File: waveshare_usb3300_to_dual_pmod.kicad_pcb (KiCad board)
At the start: 2 copper layers, 24.8 x 41.3 mm, 4 parts, among them J1 Conn_01x02_Pin, J2 PMOD, J3 PMOD, J4 Conn_02x10_Top_Bottom

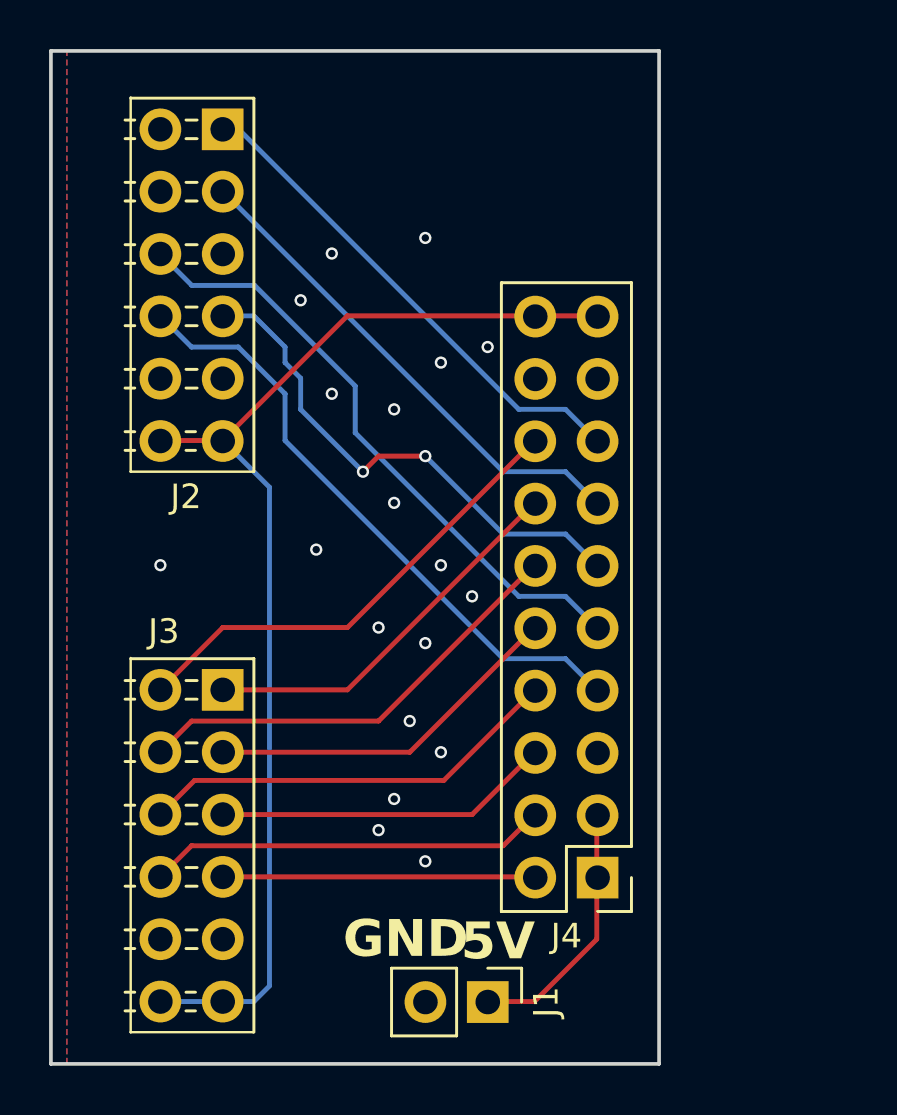
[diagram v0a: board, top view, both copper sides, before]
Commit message: waveshare_usb3300_to_dual_pmod: changed j4 footprint, resize PCB
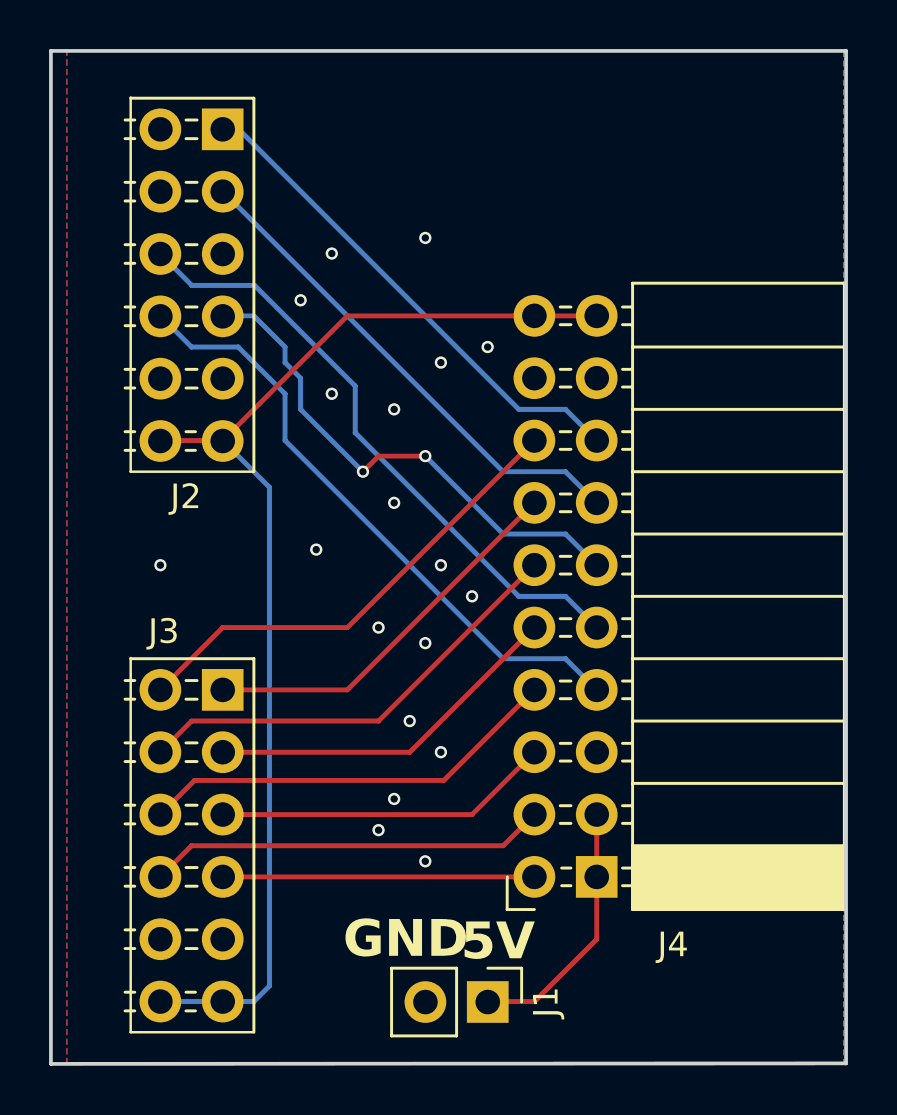
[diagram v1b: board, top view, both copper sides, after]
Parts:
- J4: footprint Connector_PinHeader_2.54mm:PinHeader_2x10_P2.54mm_Vertical -> usb3300_connector:PinSocket_2x10_P2.54mm_Horizontal
- moved J4 2.58 mm to (56.7, 56.7)
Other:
- board size 24.8 x 41.3 mm -> 32.4 x 41.3 mm

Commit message: waveshare_usb3300_to_dual_pmod.kicad_pcb: reworks GND (thanks Goran!)
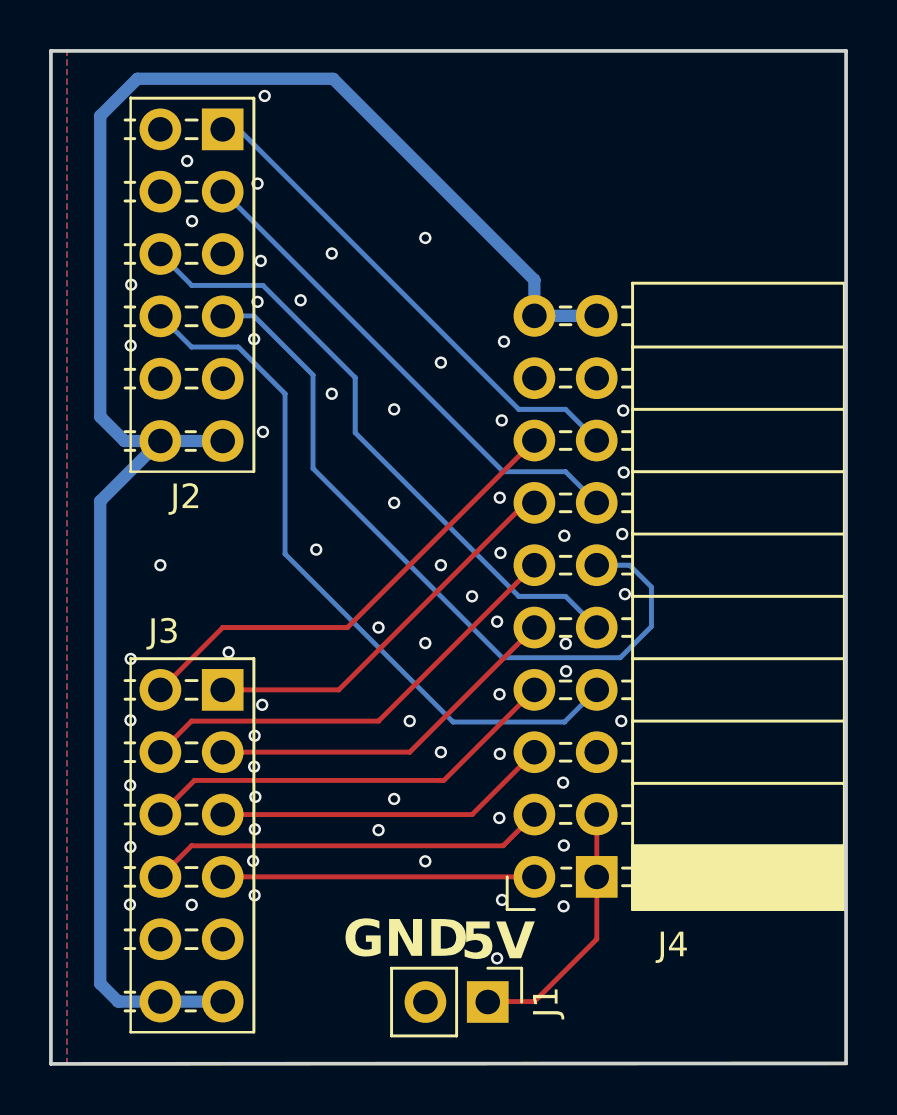
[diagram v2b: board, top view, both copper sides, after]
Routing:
- net +3.3V: track 47.6 -> 71.8 mm
- net DIR: track 21.1 -> 30.2 mm, vias 2 -> 0
- net RESET: track 25.2 -> 29.0 mm
- net GND: vias 19 -> 63

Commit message: waveshare_usb3300_to_dual_pmod.kicad_pcb: updates clock routing (thanks Goran)
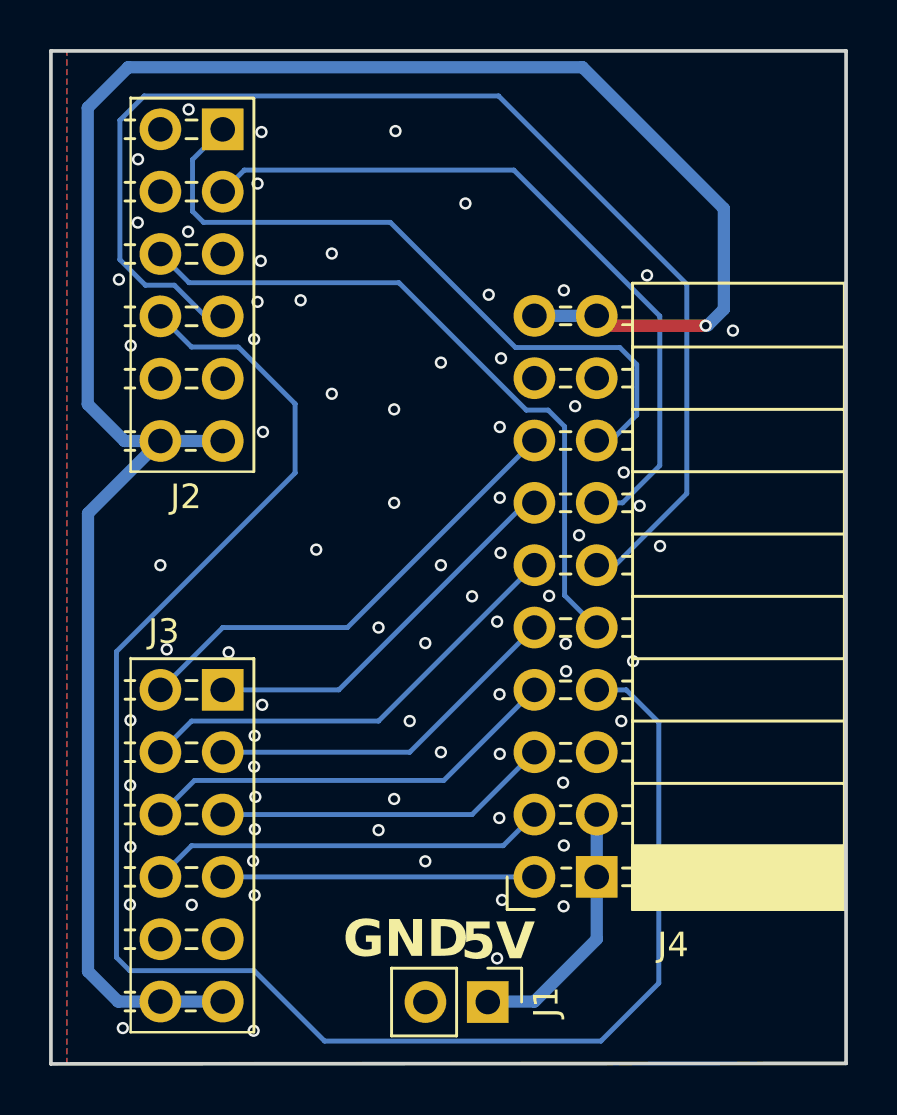
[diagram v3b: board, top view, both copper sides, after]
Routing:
- net RESET: track 29.0 -> 70.7 mm
- net DIR: track 30.2 -> 50.9 mm
- net +3.3V: track 71.8 -> 88.3 mm, vias 0 -> 1
- net NXT: track 20.5 -> 29.9 mm
- net STP: track 20.5 -> 29.2 mm
- net CLKOUT: track 25.4 -> 28.1 mm
- net GND: vias 63 -> 74
